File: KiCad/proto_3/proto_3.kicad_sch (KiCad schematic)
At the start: 12 parts

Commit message: Moving folders around
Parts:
- renumbered D1 to TVS
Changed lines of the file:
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@@
 		(on_board yes)
 		(dnp no)
-		(property "Reference" "D1"
+		(property "Reference" "TVS"
 			(at 183.896 106.426 90)
 			(effects
@@
 			(project ""
 				(path "/3ba3c426-0aff-4728-abf4-4c9cd318aec8"
-					(reference "D1")
+					(reference "TVS")
 					(unit 1)
 				)

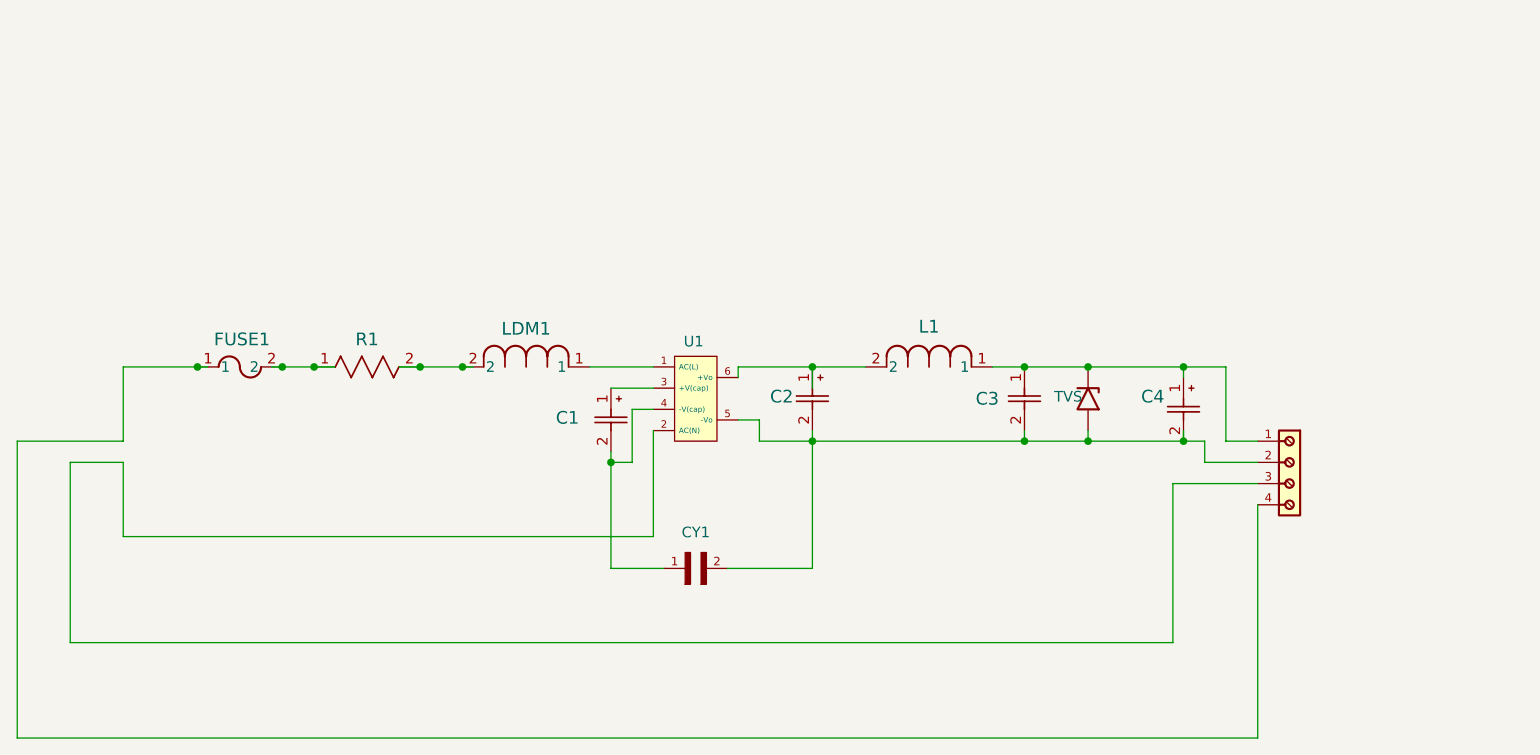
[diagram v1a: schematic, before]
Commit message: Added mounting holes and ground pour
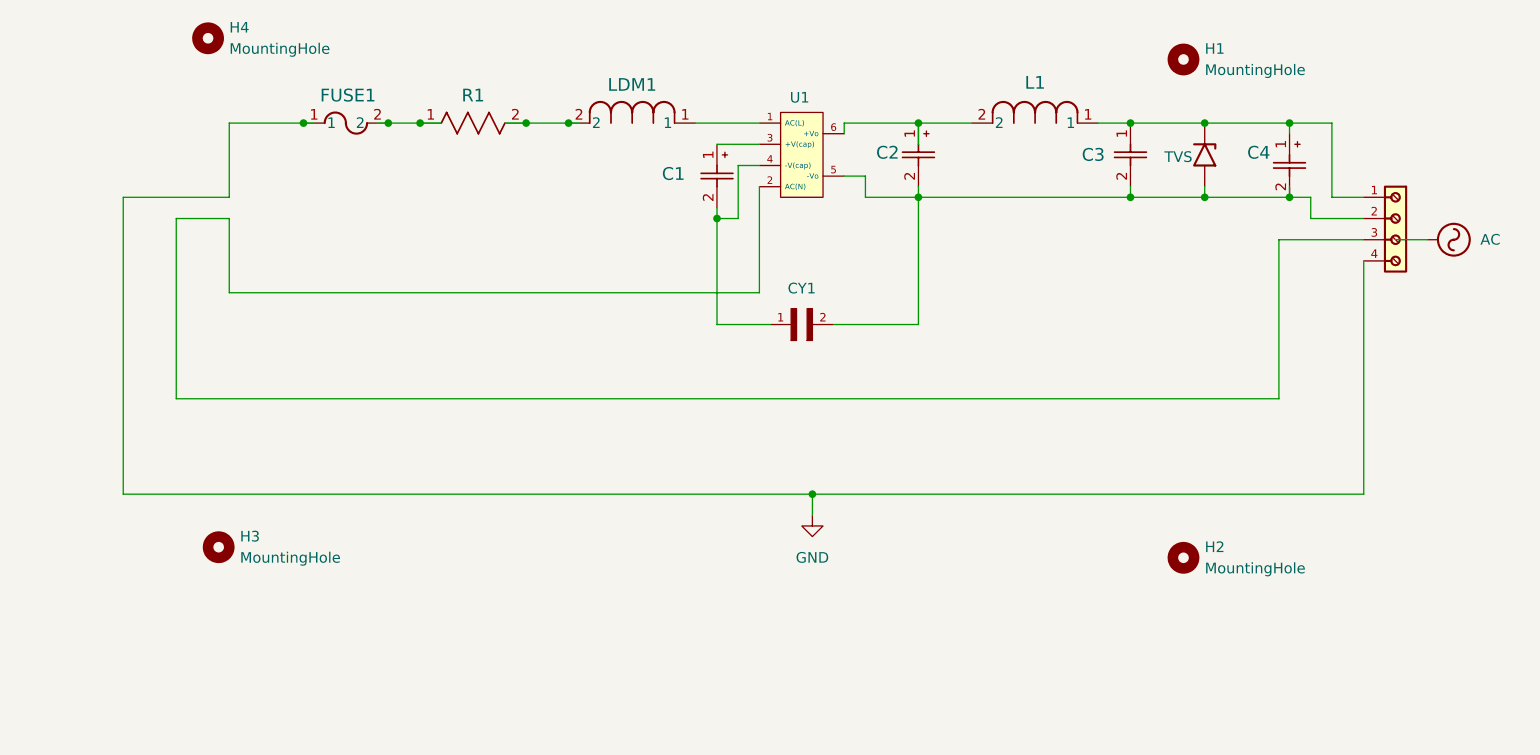
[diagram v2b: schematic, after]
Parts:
- removed TVS: SM6T6V8A, stuff:TVS_DIODE_NEW, symbol Diode:SM6T6V8A
- added D1: TVS, stuff:TVS_DIODE_NEW, symbol Diode:SM6T6V8A
- added H1, H2, H3, H4: MountingHole, MountingHole:MountingHole_2.1mm, symbol Mechanical:MountingHole
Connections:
- net at C3.1, C4.1, J1.1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: now also D1.1 (A1)
- net at C2.2, C3.2, C4.2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: now also D1.2 (A2)
- net GND: now reaches FUSE1.1, J1.4
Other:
- moved on the sheet: C1, C2, C3, C4, CY1, FUSE1, L1, LDM1, R1, U1

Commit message: seperated AC input and DC output, removed mounting holes
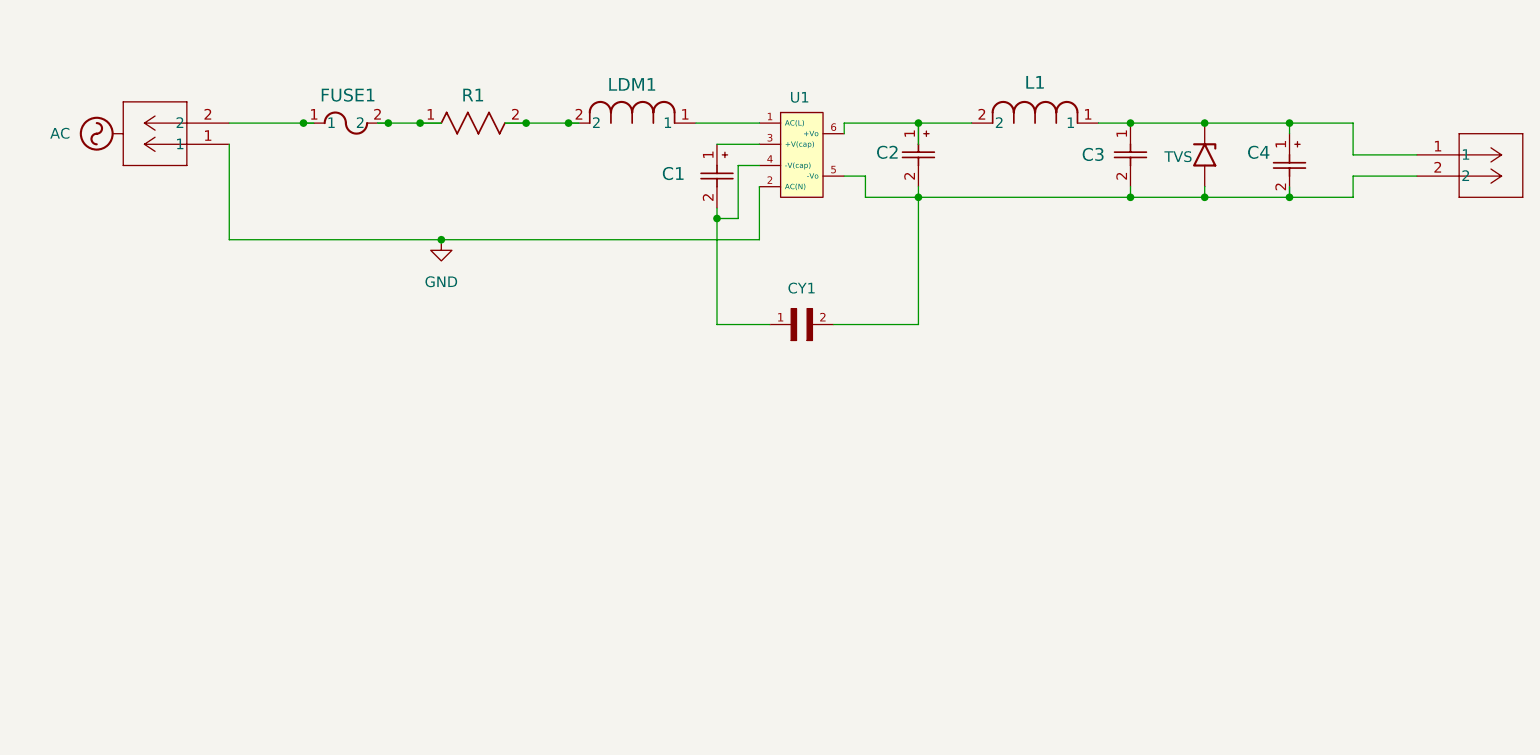
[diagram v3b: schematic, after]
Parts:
- removed H1, H2, H3, H4: MountingHole, MountingHole:MountingHole_2.1mm, symbol Mechanical:MountingHole
- removed J1: ~, stuff:screw_down_1x4, symbol 1x4_block_sym:691137710004
- added J1, J2: 1729128, CONN_1729128_PXC, symbol 1x2:1729128
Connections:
- net GND: now also U1.2 (AC(N)), J2.1; no longer FUSE1.1
- net at C3.1, C4.1, D1.1 (A1)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: now also J1.1
- net at C2.2, C3.2, C4.2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: now also J1.2
- new net: FUSE1.1, J2.2

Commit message: Added power symbols, moved ground to output rail
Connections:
- net AC: now also FUSE1.1, J2.1, J2.2, U1.2 (AC(N))
- net GND: now also C2.2, C3.2, C4.2, CY1.2, D1.2 (A2), J1.2, U1.5 (-Vo); no longer J2.1, U1.2 (AC(N))
- net +5V: now reaches C3.1, C4.1, D1.1 (A1), J1.1, L1.1
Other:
- moved on the sheet: C1, C2, C3, C4, CY1, FUSE1, L1, LDM1, R1, U1

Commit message: removed AC markings on L and N lines on AC input. Added individual L and P symbols to AC input lines. Need to create nets for each.
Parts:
- added AC(L)1: ~, symbol AC:AC_(L)
- added U2: ~, symbol AC:AC_(N)
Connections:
- net AC: no longer names the net of J2.1, U1.2 (AC(N))
- net AC: no longer FUSE1.1, J2.2
- new net: FUSE1.1, J2.2
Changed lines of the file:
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@@
-	)
-	(junction
-		(at 224.79 99.06)
-		(diameter 0)
-		(color 0 0 0 0)
 	)
 	(junction
@@
 	)
 	(junction
-		(at 76.2 92.71)
-		(diameter 0)
-		(color 0 0 0 0)
-	)
-	(junction
 		(at 119.38 92.71)
 		(diameter 0)
@@
 	)
 	(junction
-		(at 76.2 95.25)
-		(diameter 0)
-		(color 0 0 0 0)
-	)
-	(junction
 		(at 224.79 96.52)
 		(diameter 0)
@@
 	(wire
 		(pts
-			(xy 72.39 92.71) (xy 76.2 92.71)
-		)
-		(stroke
-			(width 0)
-			(type default)
-		)
-	)
-	(wire
-		(pts
 			(xy 114.3 92.71) (xy 119.38 92.71)
 		)
@@
 	(wire
 		(pts
-			(xy 72.39 95.25) (xy 76.2 95.25)
-		)
-		(stroke
-			(width 0)
-			(type default)
-		)
-	)
-	(wire
-		(pts
 			(xy 182.88 92.71) (xy 186.69 92.71)
 		)
@@
 	(wire
 		(pts
-			(xy 224.79 99.06) (xy 226.06 99.06)
-		)
-		(stroke
-			(width 0)
-			(type default)
-		)
-	)
-	(wire
-		(pts
 			(xy 142.24 100.33) (xy 142.24 106.68)
 		)
@@
 	(wire
 		(pts
-			(xy 76.2 92.71) (xy 87.63 92.71)
+			(xy 72.39 92.71) (xy 87.63 92.71)
 		)
 		(stroke
@@
 	(wire
 		(pts
-			(xy 215.9 99.06) (xy 224.79 99.06)
+			(xy 215.9 99.06) (xy 226.06 99.06)
 		)
 		(stroke
@@
 	(wire
 		(pts
-			(xy 76.2 95.25) (xy 81.28 95.25)
+			(xy 72.39 95.25) (xy 81.28 95.25)
 		)
 		(stroke
@@
 			(width 0)
 			(type default)
-		)
-	)
-	(symbol
-		(lib_id "power:PWR_FLAG")
-		(at 224.79 99.06 180)
-		(unit 1)
-		(exclude_from_sim no)
-		(in_bom yes)
-		(on_board yes)
-		(dnp no)
-		(fields_autoplaced yes)
-		(property "Reference" "#FLG02"
-			(at 224.79 100.965 0)
-			(effects
-				(font
-					(size 1.27 1.27)
-				)
-				(hide yes)
-			)
-		)
-		(property "Value" "PWR_FLAG"
-			(at 224.79 104.14 0)
-			(effects
-				(font
-					(size 1.27 1.27)
-				)
-			)
-		)
-		(property "Footprint" ""
-			(at 224.79 99.06 0)
-			(effects
-				(font
-					(size 1.27 1.27)
-				)
-				(hide yes)
-			)
-		)
-		(property "Datasheet" "~"
-			(at 224.79 99.06 0)
-			(effects
-				(font
-					(size 1.27 1.27)
-				)
-				(hide yes)
-			)
-		)
-		(property "Description" "Special symbol for telling ERC where power comes from"
-			(at 224.79 99.06 0)
-			(effects
-				(font
-					(size 1.27 1.27)
-				)
-				(hide yes)
-			)
-		)
-		(pin "1"
-		)
-		(instances
-			(project "proto_3"
-				(path "/3ba3c426-0aff-4728-abf4-4c9cd318aec8"
-					(reference "#FLG02")
-					(unit 1)
-				)
-			)
 		)
 	)
@@
 	)
 	(symbol
-		(lib_id "power:AC")
-		(at 76.2 92.71 0)
+		(lib_id "AC:AC_(N)")
+		(at 74.93 100.33 180)
 		(unit 1)
 		(exclude_from_sim no)
@@
 		(dnp no)
 		(fields_autoplaced yes)
-		(property "Reference" "#PWR01"
-			(at 76.2 95.25 0)
-			(effects
-				(font
-					(size 1.27 1.27)
-				)
-				(hide yes)
-			)
-		)
-		(property "Value" "AC"
-			(at 76.2 85.09 0)
-			(effects
-				(font
-					(size 1.27 1.27)
-				)
+		(property "Reference" "U2"
+			(at 74.93 100.33 0)
+			(effects
+				(font
+					(size 1.27 1.27)
+				)
+				(hide yes)
+			)
+		)
+		(property "Value" "~"
+			(at 80.01 97.7928 0)
+			(effects
+				(font
+					(size 1.27 1.27)
+				)
+				(justify right)
 			)
 		)
 		(property "Footprint" ""
-			(at 76.2 92.71 0)
+			(at 74.93 100.33 0)
 			(effects
 				(font
@@
 		)
 		(property "Datasheet" ""
-			(at 76.2 92.71 0)
-			(effects
-				(font
-					(size 1.27 1.27)
-				)
-				(hide yes)
-			)
-		)
-		(property "Description" "Power symbol creates a global label with name \"AC\""
-			(at 76.2 92.71 0)
-			(effects
-				(font
-					(size 1.27 1.27)
-				)
-				(hide yes)
-			)
-		)
-		(pin "1"
+			(at 74.93 100.33 0)
+			(effects
+				(font
+					(size 1.27 1.27)
+				)
+				(hide yes)
+			)
+		)
+		(property "Description" ""
+			(at 74.93 100.33 0)
+			(effects
+				(font
+					(size 1.27 1.27)
+				)
+				(hide yes)
+			)
 		)
 		(instances
-			(project "proto_3"
+			(project ""
 				(path "/3ba3c426-0aff-4728-abf4-4c9cd318aec8"
-					(reference "#PWR01")
+					(reference "U2")
 					(unit 1)
 				)
@@
 	)
 	(symbol
+		(lib_id "AC:AC_(L)")
+		(at 74.93 87.63 0)
+		(unit 1)
+		(exclude_from_sim no)
+		(in_bom yes)
+		(on_board yes)
+		(dnp no)
+		(fields_autoplaced yes)
+		(property "Reference" "AC(L)1"
+			(at 74.93 87.63 0)
+			(effects
+				(font
+					(size 1.27 1.27)
+				)
+				(hide yes)
+			)
+		)
+		(property "Value" "~"
+			(at 80.01 90.17 0)
+			(effects
+				(font
+					(size 1.27 1.27)
+				)
+				(justify left)
+			)
+		)
+		(property "Footprint" ""
+			(at 74.93 87.63 0)
+			(effects
+				(font
+					(size 1.27 1.27)
+				)
+				(hide yes)
+			)
+		)
+		(property "Datasheet" ""
+			(at 74.93 87.63 0)
+			(effects
+				(font
+					(size 1.27 1.27)
+				)
+				(hide yes)
+			)
+		)
+		(property "Description" ""
+			(at 74.93 87.63 0)
+			(effects
+				(font
+					(size 1.27 1.27)
+				)
+				(hide yes)
+			)
+		)
+		(instances
+			(project "proto_3"
+				(path "/3ba3c426-0aff-4728-abf4-4c9cd318aec8"
+					(reference "AC(L)1")
+					(unit 1)
+				)
+			)
+		)
+	)
+	(symbol
 		(lib_id "Inductor-4.7uH/60ohm:RLB9012-4R7ML")
 		(at 167.64 92.71 0)
@@
 					(unit 1)
 				)
-			)
-		)
-	)
-	(symbol
-		(lib_id "power:AC")
-		(at 76.2 95.25 180)
-		(unit 1)
-		(exclude_from_sim no)
-		(in_bom yes)
-		(on_board yes)
-		(dnp no)
-		(fields_autoplaced yes)
-		(property "Reference" "#PWR04"
-			(at 76.2 92.71 0)
-			(effects
-				(font
-					(size 1.27 1.27)
-				)
-				(hide yes)
-			)
-		)
-		(property "Value" "AC"
-			(at 76.2 102.87 0)
-			(effects
-				(font
-					(size 1.27 1.27)
-				)
-			)
-		)
-		(property "Footprint" ""
-			(at 76.2 95.25 0)
-			(effects
-				(font
-					(size 1.27 1.27)
-				)
-				(hide yes)
-			)
-		)
-		(property "Datasheet" ""
-			(at 76.2 95.25 0)
-			(effects
-				(font
-					(size 1.27 1.27)
-				)
-				(hide yes)
-			)
-		)
-		(property "Description" "Power symbol creates a global label with name \"AC\""
-			(at 76.2 95.25 0)
-			(effects
-				(font
-					(size 1.27 1.27)
-				)
-				(hide yes)
-			)
-		)
-		(pin "1"
-		)
-		(instances
-			(project "proto_3"
-				(path "/3ba3c426-0aff-4728-abf4-4c9cd318aec8"
-					(reference "#PWR04")
-					(unit 1)
-				)

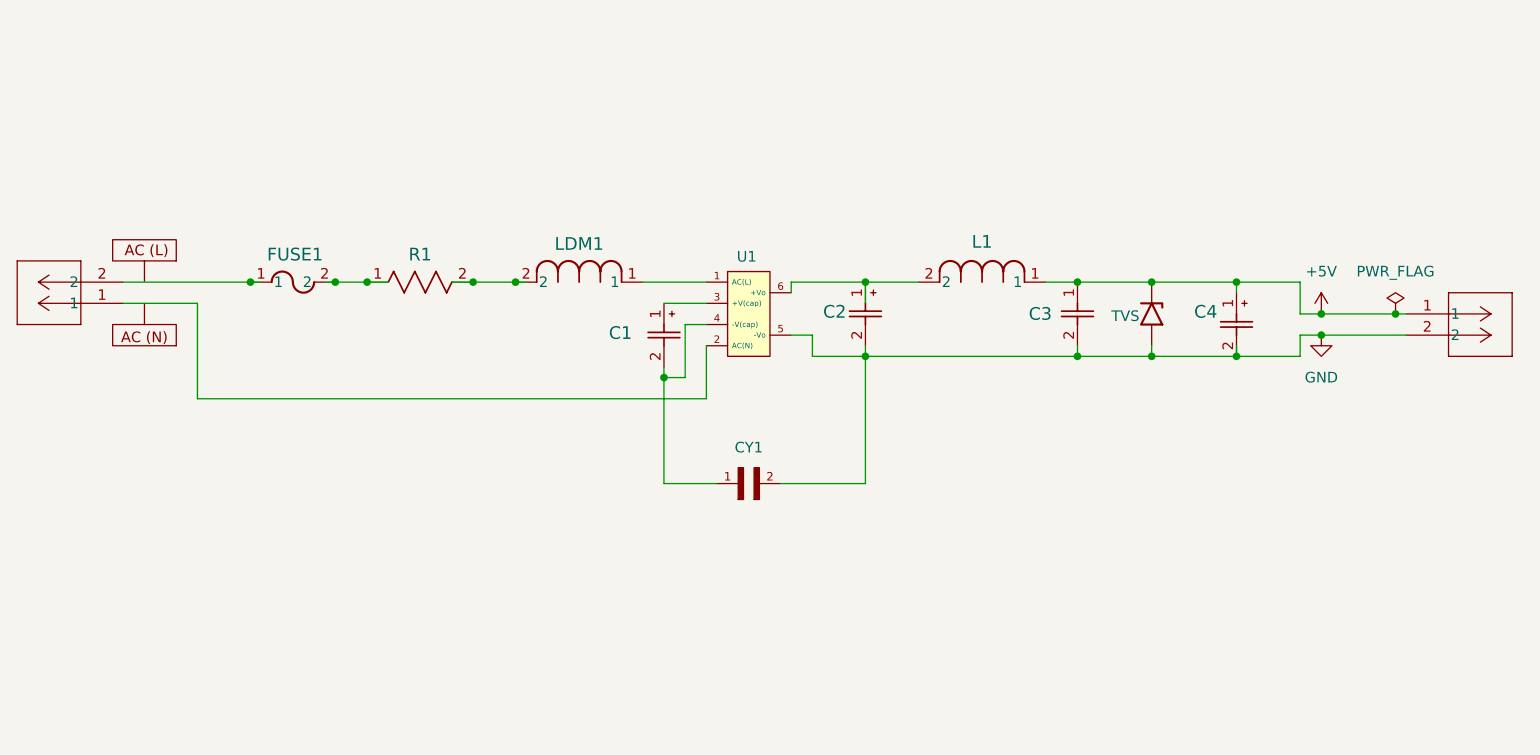
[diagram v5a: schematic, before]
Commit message: labeled nets and netclasses for organization
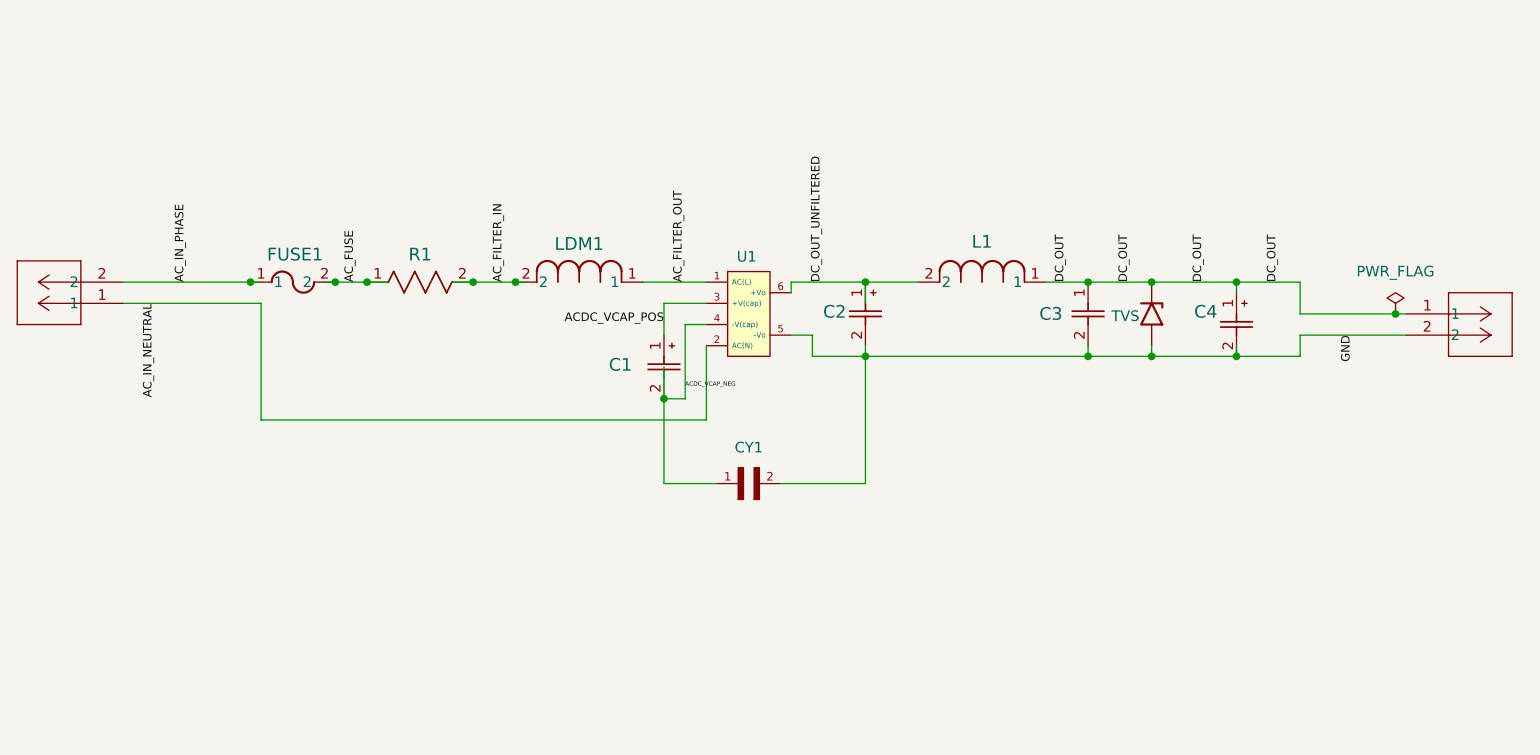
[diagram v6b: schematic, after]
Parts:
- removed AC(L)1: ~, symbol AC:AC_(L)
- removed U2: ~, symbol AC:AC_(N)
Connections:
- net AC_FILTER_OUT: now reaches LDM1.1, U1.1 (AC(L))
- net AC_FILTER_IN: now reaches LDM1.2, R1.2
- net AC_IN_NEUTRAL: now reaches J2.1, U1.2 (AC(N))
- net AC_IN_PHASE: now reaches FUSE1.1, J2.2
- net ACDC_VCAP_POS: now reaches C1.1, U1.3 (+V(cap))
- net ACDC_VCAP_NEG: now reaches C1.2, CY1.1, U1.4 (-V(cap))
- net DC_OUT_UNFILTERED: now reaches C2.1, L1.2, U1.6 (+Vo)
- net AC_FUSE: now reaches FUSE1.2, R1.1
- net +5V renamed DC_OUT
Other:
- moved on the sheet: C1, C3

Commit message: Added new footprint for transformer to pcb
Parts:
- U1: footprint stuff:transformer_MPL-05SC-F -> stuff:transformer_MPL-05SC-F_new
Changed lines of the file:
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@@
 			)
 		)
-		(property "Footprint" "stuff:transformer_MPL-05SC-F"
+		(property "Footprint" "stuff:transformer_MPL-05SC-F_new"
 			(at 147.574 101.346 0)
 			(effects
